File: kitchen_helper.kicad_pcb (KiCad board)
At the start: 2 copper layers, 92 x 62.1 mm, 62 parts, among them IC1 ESP32-S3-WROOM-1-N8R8, IC2 FS312F-G, IC3 VReg 3v3, J1 Temp 1, J2 PROG_HDR, J3 Temp 2, J4 DISP_HDR, J6 Charger, J7 Battery, Q1 SS8050-G, Q2 SS8050-G, Q3 SS8050-G, Q4 SS8050-G, Q5 SS8050-G, Q6 FS8205, SW1 SW_Reset, SW2 BTN_LEFT, SW3 BTN_RIGHT, SW4 RotaryEncoder_Switch

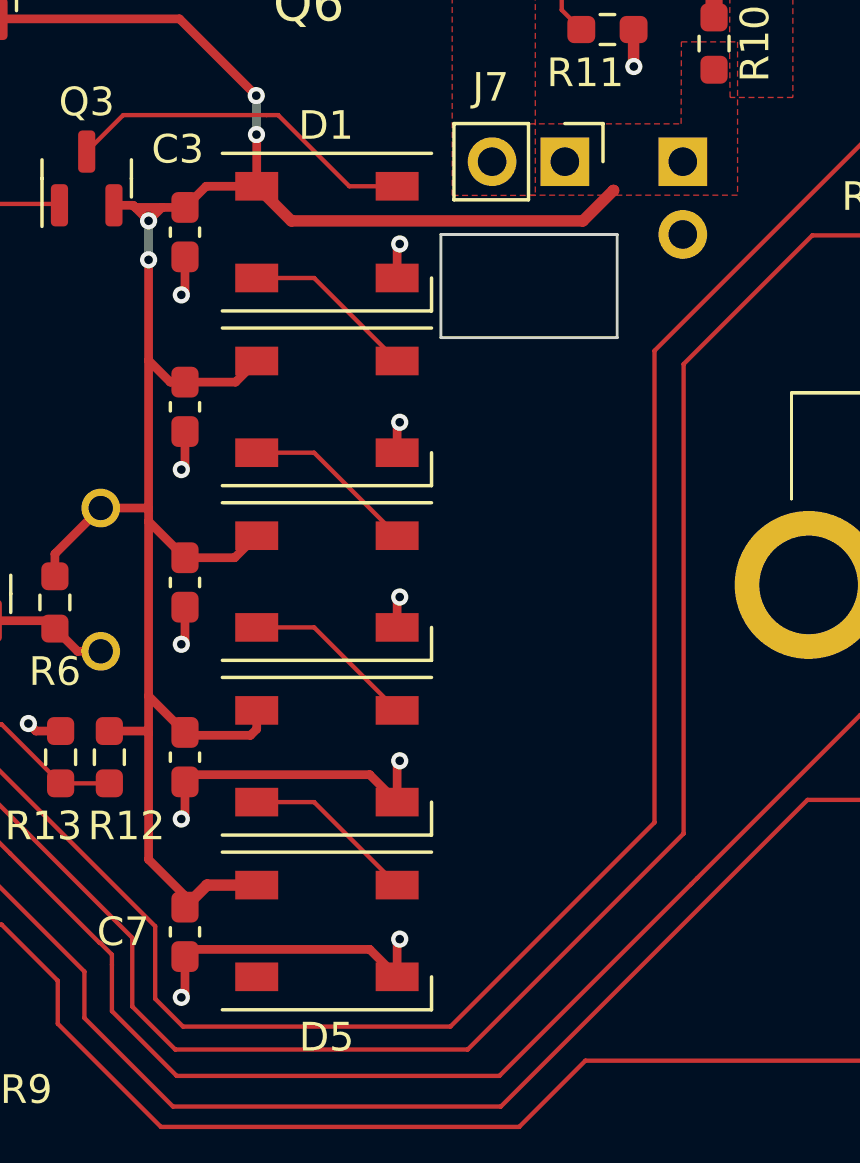
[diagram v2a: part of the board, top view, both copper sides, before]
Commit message: Migrated project to KiCad7
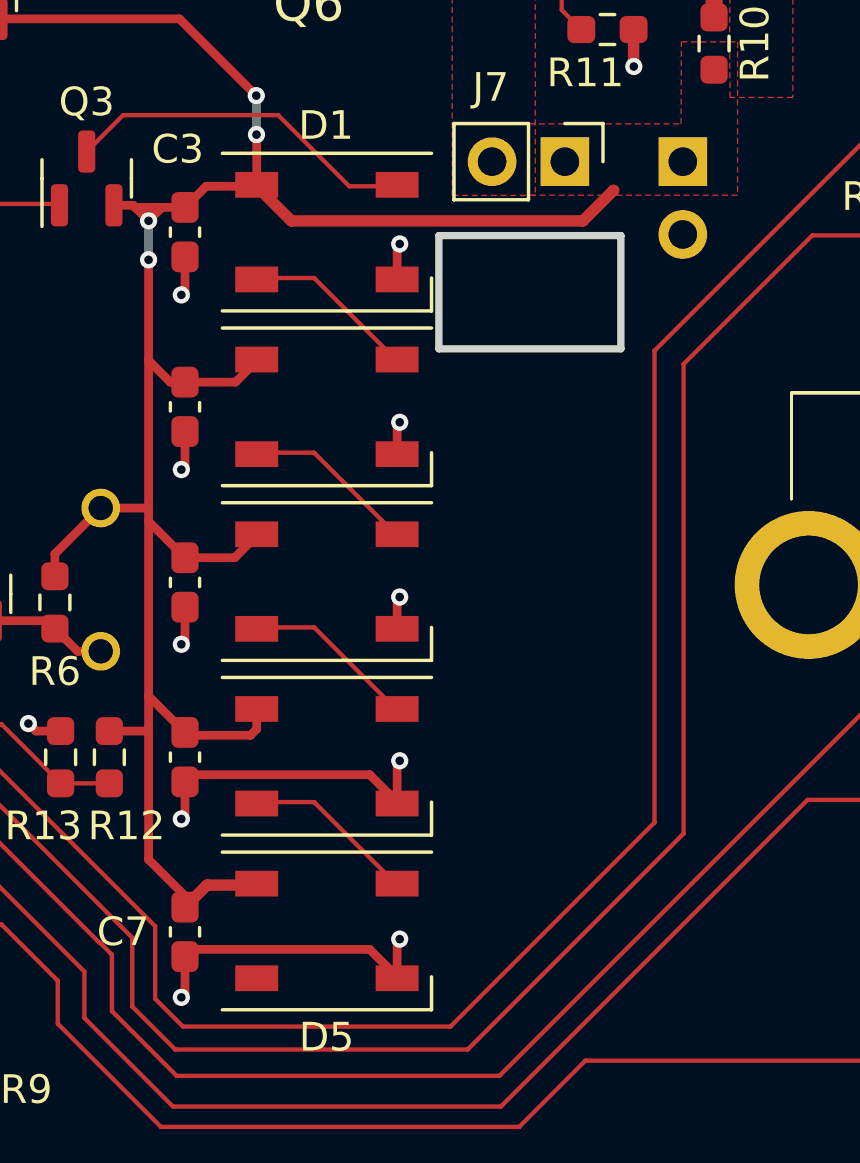
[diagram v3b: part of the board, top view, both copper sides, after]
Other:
- outline, holes or cut-outs redrawn
